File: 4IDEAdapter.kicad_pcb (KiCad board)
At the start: 2 copper layers, 78.7 x 68.6 mm, 13 parts

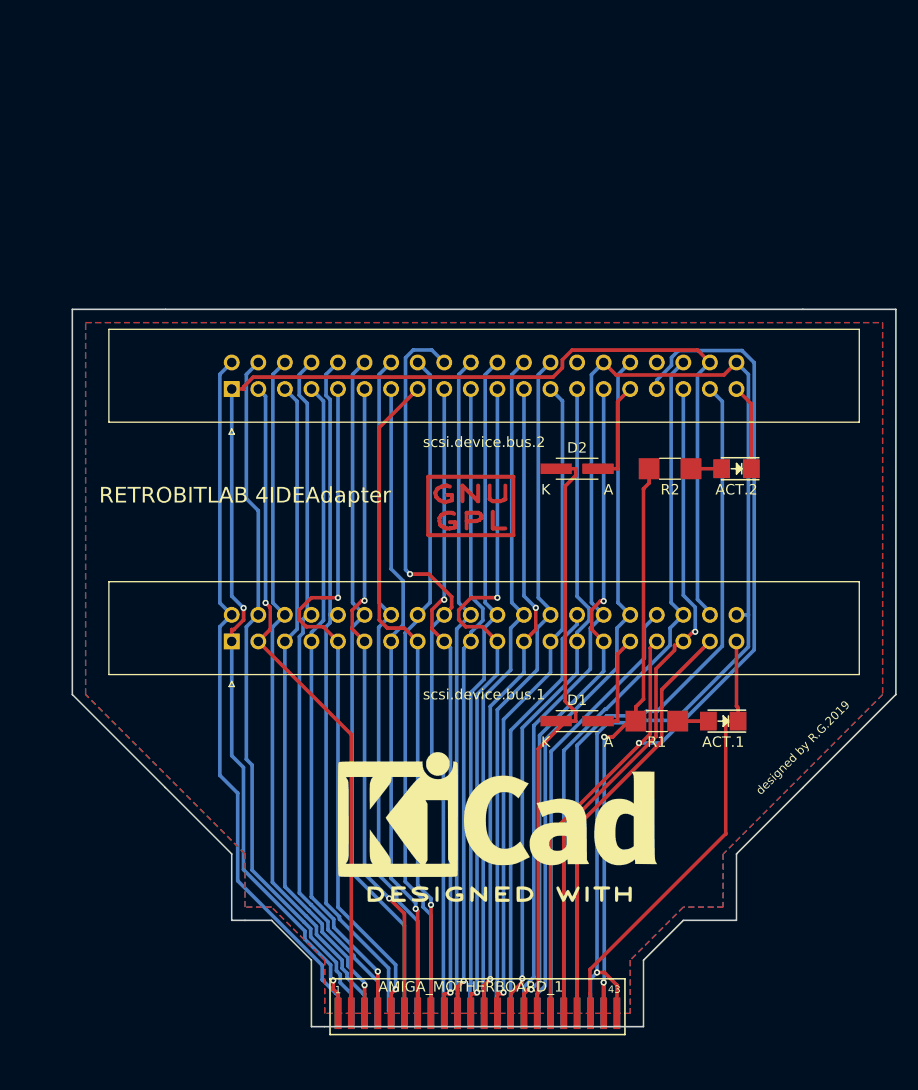
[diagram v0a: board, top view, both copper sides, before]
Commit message: added a second ide port 44 pin
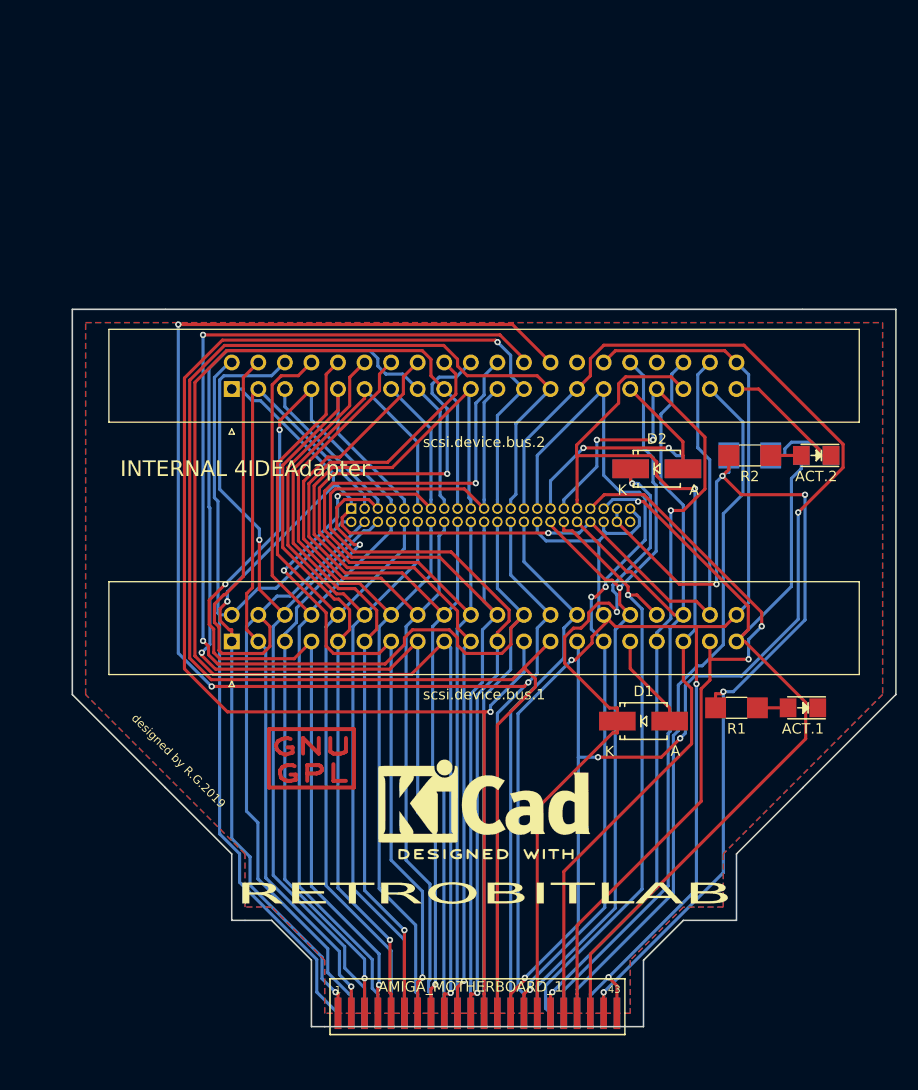
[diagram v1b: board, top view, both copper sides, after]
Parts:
- removed GPL: Symbol_GNU-GPL_CopperTop_Small, Symbol:Symbol_GNU-GPL_CopperTop_Small
- removed the REF** at (157.5, 111.8)
- added ACT.3: LED, LEDs:LED_1206, B.Cu at (188.0, 77.5)
- added D3: D, Diodes_SMD:SMA_Handsoldering, B.Cu at (172.7, 78.7)
- added GPLLOGO: Symbol_GNU-GPL_CopperTop_Small, Symbol:Symbol_GNU-GPL_CopperTop_Small, F.Cu at (139.7, 106.7)
- added R3: 330, Resistors_SMD:R_1210_HandSoldering, B.Cu at (181.6, 77.5)
- added REF**: KiCad-Logo2_8mm_SilkScreen, Symbol:KiCad-Logo2_8mm_SilkScreen, F.Cu at (156.2, 110.5)
- added scsi.device.44pin.1: conn_CONN_02X22, RetroBitLab:PinHeader_2x22_P1.27mm_Vertical, B.Cu at (143.5, 82.5)
- moved G*** 29.6 mm to (124.5, 85.1), turned to 270 degrees
- moved ACT.1 7.73 mm to (186.7, 101.6)
- moved R1 7.73 mm to (180.3, 101.6)
- moved ACT.2 7.73 mm to (188.0, 77.5)
- moved R2 7.73 mm to (181.6, 77.5)
- moved D2 7.62 mm to (172.7, 78.7)
- moved D1 6.35 mm to (171.4, 102.9)
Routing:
- net /A27: track 65.4 -> 154.1 mm, vias 0 -> 3
- net /A13: track 63.0 -> 149.4 mm, vias 1 -> 0
- net /A26: track 64.8 -> 148.5 mm, vias 0 -> 2
- net /A12: track 62.2 -> 145.2 mm
- net /A14: track 63.3 -> 131.5 mm, vias 1 -> 4
- net /A9: track 61.6 -> 127.9 mm, vias 2 -> 1
- net /A8: track 64.2 -> 121.6 mm, vias 1 -> 2
- net /A39: track 42.2 -> 91.0 mm, vias 0 -> 1
- net +5V: track 58.0 -> 99.4 mm, vias 2 -> 5
- net /A25: track 64.3 -> 99.4 mm, vias 0 -> 1
- net /A24: track 63.8 -> 96.0 mm, vias 0 -> 1
- net /A37: track 40.8 -> 71.1 mm, vias 0 -> 2
- net /A10: track 61.2 -> 91.3 mm
- net /A4: track 63.3 -> 92.6 mm, vias 1 -> 3
- net /A16: track 67.8 -> 94.9 mm
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- added copper zone on F.Cu, net +5V
- removed copper zone on F.Cu, net GND
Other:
- net class Default: trace_width 0.35 -> 0.3
- board text added: "INTERNAL 4IDEAdapter"
- board text added: "RETROBITLAB"
- board text removed: "RETROBITLAB 4IDEAdapter"

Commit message: Updated connectors
The IDE44 pin connector was wrong. Due to the complexity of having 3
connectors on board the size of the board need to be increased. Now it
is almost like a Credit Card Size. It needs an Amiga 1200 or Amiga 600
placed into a TowerCase and *NOT TOO NEAR* to the bottom of the case...
But if you need a 4 devices connected, for sure the default case has not
accomplishes that!
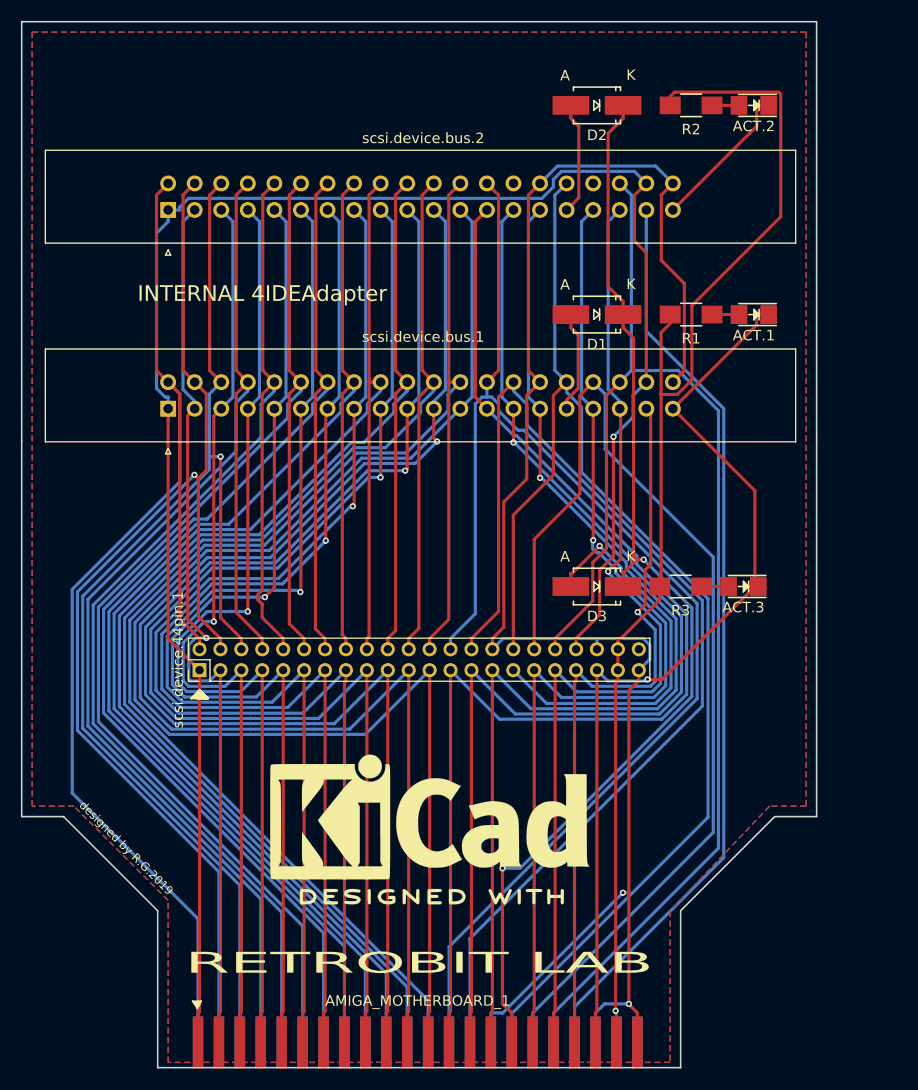
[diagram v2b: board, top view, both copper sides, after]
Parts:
- removed GPLLOGO: Symbol_GNU-GPL_CopperTop_Small, Symbol:Symbol_GNU-GPL_CopperTop_Small
- removed the REF** at (156.2, 110.5)
- added REF**: KiCad-Logo2_12mm_SilkScreen, Symbol:KiCad-Logo2_12mm_SilkScreen, F.Cu at (151.0, 112.0)
- ACT.3, D3: moved to F.Cu
- AMIGA_MOTHERBOARD_1: footprint RetroBitLab:Vertical_IDE_44_Pins_2x22_1.27_PCB -> RetroBitLab:Socket_IDC_2x22_2.00mm_PCB
- R1, R2: footprint Resistors_SMD:R_1210_HandSoldering -> Resistors_SMD:R_1206_HandSoldering
- R3: footprint Resistors_SMD:R_1210_HandSoldering -> Resistors_SMD:R_1206_HandSoldering; moved to F.Cu
- scsi.device.44pin.1: footprint RetroBitLab:PinHeader_2x22_P1.27mm_Vertical -> RetroBitLab:PinHeader_2x22_P2.00mm_Vertical; moved to F.Cu
- moved D1 39.1 mm to (167.0, 64.0), turned to 180 degrees
- moved ACT.1 37.9 mm to (182.0, 64.0)
- moved R1 37.8 mm to (176.0, 64.0)
- moved D2 35.2 mm to (167.0, 44.0), turned to 180 degrees
- moved ACT.2 34.0 mm to (182.0, 44.0)
- moved R2 33.9 mm to (176.0, 44.0)
- moved G*** 26.6 mm to (151.0, 86.0), turned to 180 degrees
- moved scsi.device.bus.1 23.1 mm to (126.0, 73.0)
- moved scsi.device.44pin.1 21.2 mm to (129.0, 98.0), turned to 90 degrees
- moved scsi.device.bus.2 18.2 mm to (126.0, 54.0)
- moved ACT.3 14.3 mm to (181.0, 90.0), turned to 180 degrees
- moved R3 14.2 mm to (175.0, 90.0)
- moved D3 12.6 mm to (167.0, 90.0), turned to 180 degrees
- moved AMIGA_MOTHERBOARD_1 7.18 mm to (149.9, 134.6)
- moved G*** 6.03 mm to (149.0, 112.0)
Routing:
- net /A28: track 51.7 -> 107.0 mm
- net /A32: track 78.2 -> 124.1 mm, vias 1 -> 0
- net /A34: track 58.1 -> 102.9 mm, vias 1 -> 0
- net /A21: track 83.1 -> 127.8 mm
- net /A22: track 85.6 -> 130.1 mm
- net /A20: track 82.2 -> 125.8 mm
- net /A19: track 81.6 -> 124.9 mm
- net /A36: track 82.6 -> 124.9 mm
- net /A23: track 90.6 -> 132.8 mm
- net /A18: track 81.9 -> 123.3 mm
- net /A24: track 96.0 -> 135.4 mm, vias 1 -> 0
- net /A11: track 91.6 -> 130.7 mm
- net /A31: track 67.0 -> 105.9 mm
- net /A25: track 99.4 -> 138.1 mm, vias 1 -> 0
- net /A15: track 84.2 -> 119.6 mm
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- added copper zone on F.Cu, net GND
- removed copper zone on F.Cu, net +5V
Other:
- board size 78.7 x 68.6 mm -> 76 x 100 mm
- board text added: "RETROBIT LAB"
- board text removed: "RETROBITLAB"

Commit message: added activity led management
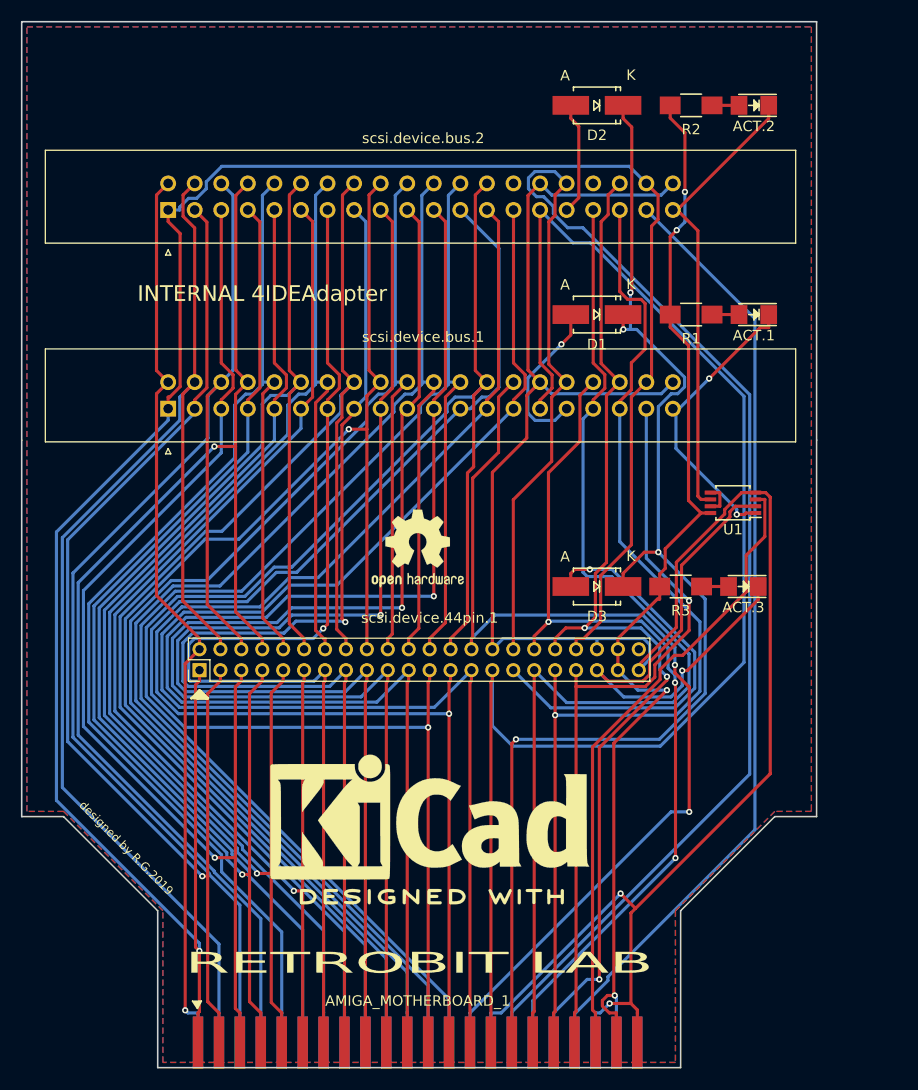
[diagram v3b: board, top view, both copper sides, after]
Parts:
- added REF**: OSHW-Logo2_9.8x8mm_SilkScreen, Symbol:OSHW-Logo2_9.8x8mm_SilkScreen, F.Cu at (149.9, 86.4)
- added U1: 74LVC2G08, Housings_SSOP:TSSOP-8_3x3mm_Pitch0.65mm, F.Cu at (180.0, 82.0)
- D1, D2, D3: value D -> 1N4148
- renumbered G*** to AMIGALOGO, REF** to WBLOGO
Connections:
- net Net-(ACT.2-Pad1) renamed /A39scsi.2
- ACT.1 pad 1: /A39 -> /A39scsi.1
- ACT.3 pad 1: /A39 -> /A39scsi.0
- scsi.device.44pin.1 pad 39: /A39 -> /A39scsi.0
- scsi.device.bus.1 pad 39: /A39 -> /A39scsi.1
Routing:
- net /A39scsi.0: track 0.00 -> 49.6 mm, vias 0 -> 1
- net GND: track 165.4 -> 204.7 mm
- net /A1: track 178.6 -> 215.3 mm
- net /A29: track 107.8 -> 141.4 mm, vias 1 -> 0
- net /A15: track 119.6 -> 86.9 mm, vias 0 -> 1
- net /A32: track 124.1 -> 154.5 mm
- net /A39scsi.2: track 14.5 -> 43.6 mm
- net /A39: track 89.0 -> 60.3 mm, vias 1 -> 0
- net /A39scsi.1: track 0.00 -> 27.9 mm, vias 0 -> 2
- net /A2: track 87.3 -> 112.1 mm
- net /A36: track 124.9 -> 100.9 mm, vias 0 -> 3
- net /A14: track 112.1 -> 135.2 mm, vias 1 -> 0
- net /A3: track 90.1 -> 111.5 mm
- net /A34: track 102.9 -> 84.1 mm, vias 0 -> 3
- net /A4: track 96.1 -> 113.7 mm
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
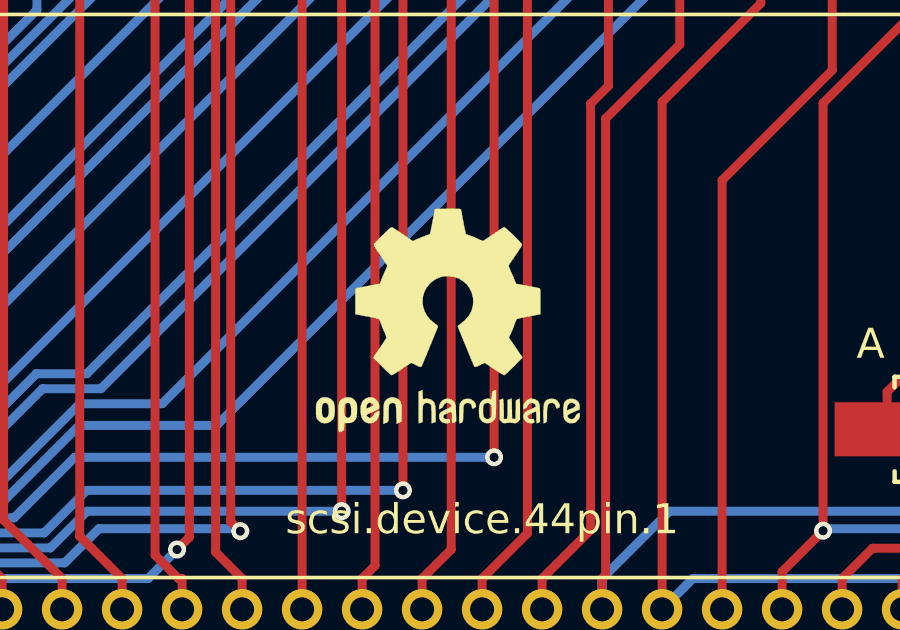
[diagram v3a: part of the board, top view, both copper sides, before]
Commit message: Modified silkscreen
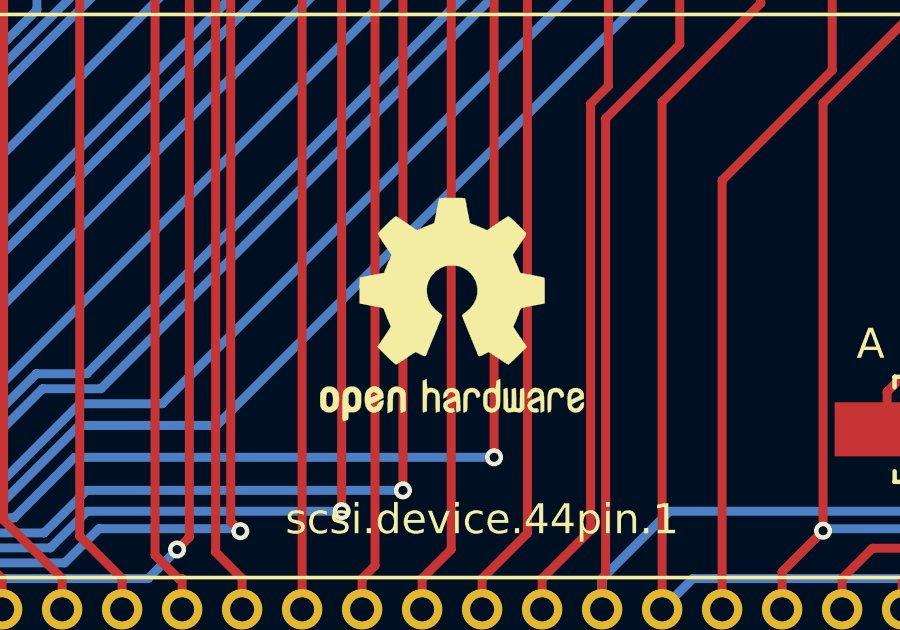
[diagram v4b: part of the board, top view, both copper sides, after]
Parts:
- removed AMIGALOGO: LOGO, RetroBitLab:amigaLogo_BW_31x12mm-SilkScreenBack
- removed the G*** at (149.0, 112.0)
- added G***: LOGO, RetroBitLab:amigaLogo_BW_31x12mm, B.Cu at (149.0, 85.0)
- added G***: LOGO, RetroBitLab:amigaWorkBench1, B.Cu at (152.0, 111.0)
- moved REF** 0.39 mm to (150.0, 86.0)
